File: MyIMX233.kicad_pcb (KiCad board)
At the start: 2 copper layers, 74.1 x 92 mm, 40 parts, among them IC1 iMX233, IC2 DDR_SDRAM_MT46_x16, J1 USB_A, J2 Micro_SD_Card, SW1 SWITCH_PUSHBUTTON, Y1 24Mhz

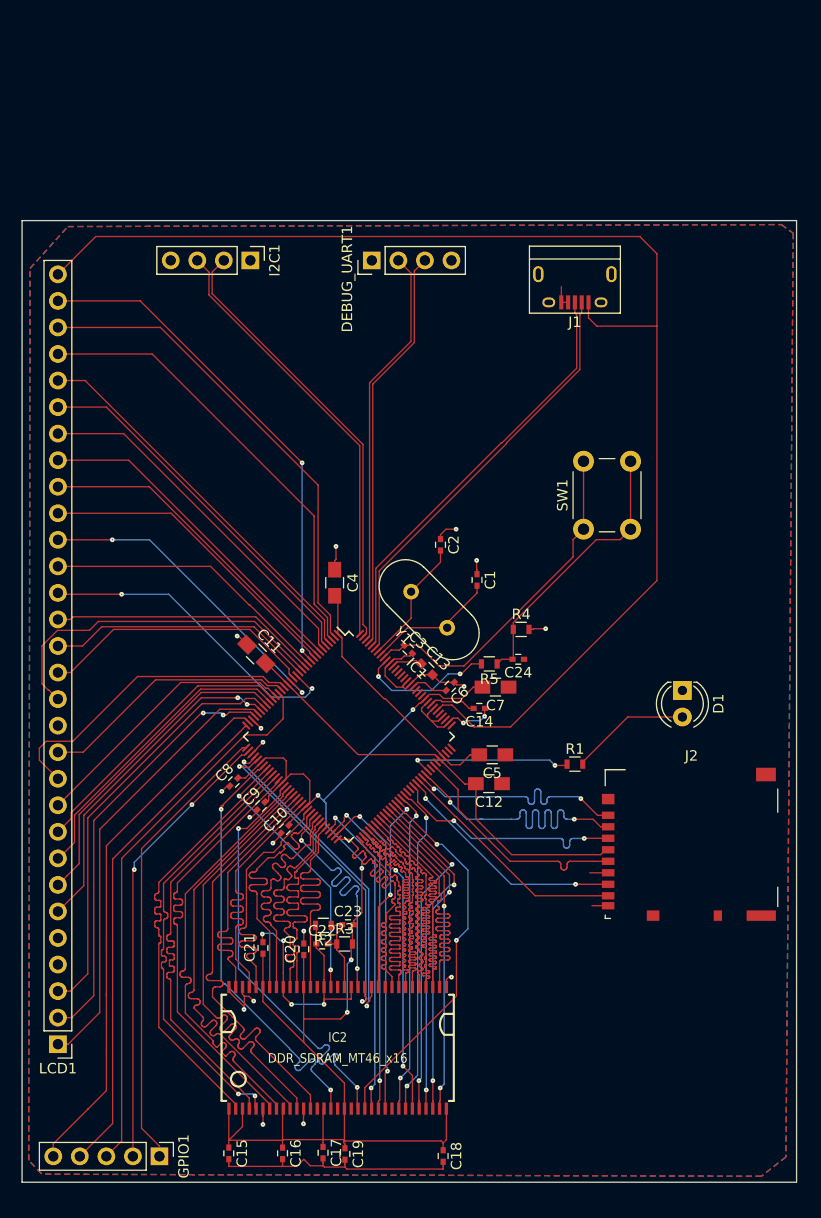
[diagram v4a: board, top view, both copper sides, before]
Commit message: updated with step files new battery and inductor diag
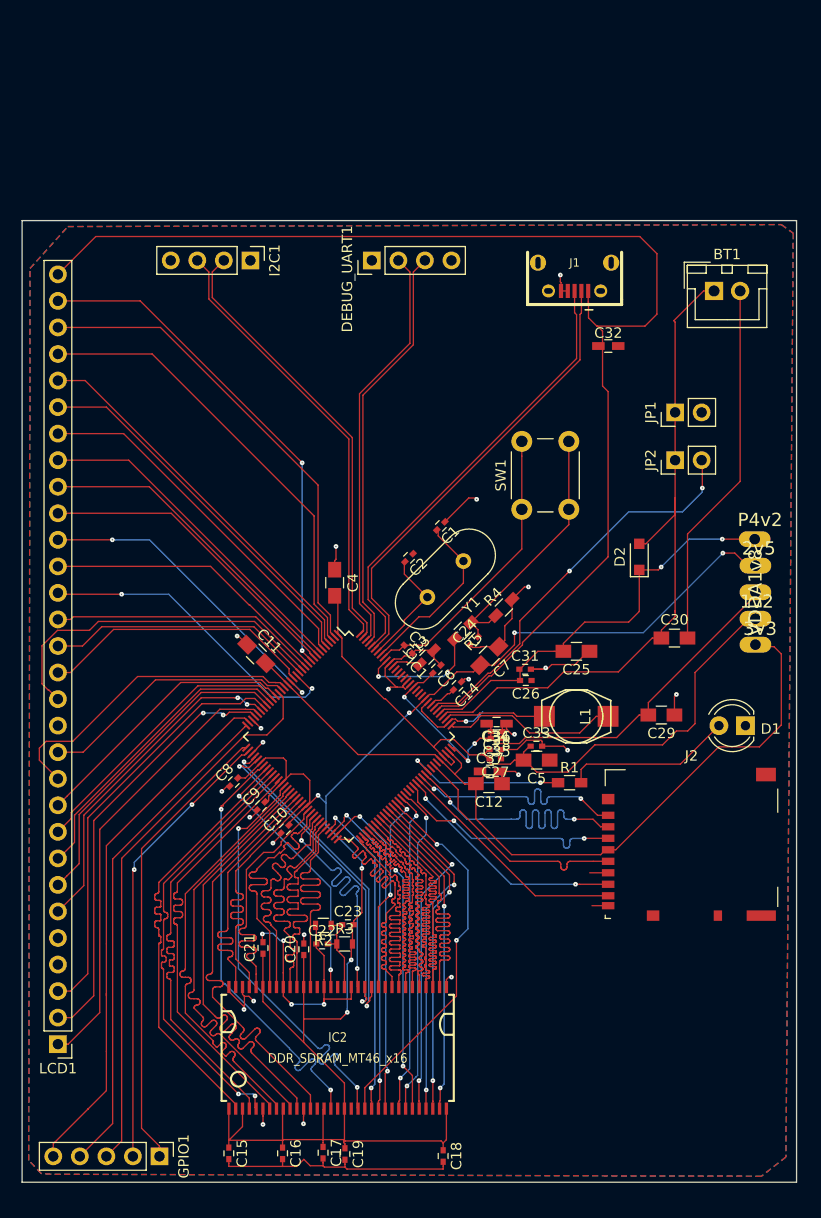
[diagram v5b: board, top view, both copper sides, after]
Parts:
- added BT1: Battery, Connectors_JST:JST_XH_B02B-XH-A_02x2.50mm_Straight, F.Cu at (131.9, 56.3)
- added C25: 22u, Capacitors_SMD:C_0805_HandSoldering, F.Cu at (118.8, 90.7)
- added C26: 1u, Capacitors_SMD:C_0402, F.Cu at (113.9, 93.5)
- added C27: 1u, Capacitors_SMD:C_0402, F.Cu at (111.0, 101.0)
- added C28: 10n, Capacitors_SMD:C_0402, F.Cu at (111.1, 98.4)
- added C29: 47u, Capacitors_SMD:C_0805_HandSoldering, F.Cu at (126.9, 96.8)
- added C30: 47u, Capacitors_SMD:C_0805_HandSoldering, F.Cu at (128.1, 89.5)
- added C31: 100n, Capacitors_SMD:C_0402, F.Cu at (113.9, 92.5)
- added C32: 4.7uf, Capacitors_SMD:C_0603_HandSoldering, F.Cu at (121.8, 61.5)
- added C33: 100n, Capacitors_SMD:C_0402, F.Cu at (114.9, 99.8)
- added C34: 10n, Capacitors_SMD:C_0402, F.Cu at (111.0, 100.1)
- added C35: 100n, Capacitors_SMD:C_0402, F.Cu at (111.1, 99.1)
- added C36: 1u, Capacitors_SMD:C_0603_HandSoldering, F.Cu at (111.1, 97.7)
- added C37: 1u, Capacitors_SMD:C_0603_HandSoldering, F.Cu at (110.5, 102.2)
- added D2: D_Schottky, Diodes_SMD:D_SOD-323_HandSoldering, F.Cu at (124.8, 81.7)
- added JP1: Jumper, Pin_Headers:Pin_Header_Straight_1x02_Pitch2.54mm, F.Cu at (128.2, 67.9)
- added JP2: Jumper, Pin_Headers:Pin_Header_Straight_1x02_Pitch2.54mm, F.Cu at (128.2, 72.5)
- added L1: 22uH, mylib:Bourns22uh6x6mm, F.Cu at (118.7, 97.0)
- added P1: P4v2, iMX233-OLinuXino-NANO_Rev_B:GOGO_TESTPAD40_OBLONG, F.Cu at (135.8, 80.0)
- added P2: 1v2, iMX233-OLinuXino-NANO_Rev_B:GOGO_TESTPAD40_OBLONG, F.Cu at (135.9, 87.6)
- added P3: VDDA1v8, iMX233-OLinuXino-NANO_Rev_B:GOGO_TESTPAD40_OBLONG, F.Cu at (135.9, 85.1)
- added P4: 2v5, iMX233-OLinuXino-NANO_Rev_B:GOGO_TESTPAD40_OBLONG, F.Cu at (135.9, 82.5)
- added P5: 3v3, iMX233-OLinuXino-NANO_Rev_B:GOGO_TESTPAD40_OBLONG, F.Cu at (135.9, 90.1)
- C12: value 22u -> 100n
- C13: footprint Capacitors_SMD:C_0603 -> Capacitors_SMD:C_0603_HandSoldering
- IC2: footprint opendous:TSOP66_JEDEC_DDR_SDRAM -> mylib:TSOP66_JEDEC_DDR_SDRAM
- J1: footprint mylib:USB_Micro-B_MOLEX_105017-0001 -> conn-fci:CONN-10118194-0001LF-FCI
- R1, R4, R5: footprint Resistors_SMD:R_0603 -> Resistors_SMD:R_0603_HandSoldering
- moved D1 6.91 mm to (134.9, 97.9), turned to 180 degrees
- moved Y1 6.57 mm to (108.0, 82.1), turned to 225 degrees
- moved C1 6.23 mm to (105.8, 78.7), turned to 225 degrees
- moved SW1 6.21 mm to (113.5, 77.2)
- moved C24 4.60 mm to (109.0, 89.7), turned to 45 degrees
- moved C5 4.27 mm to (115.0, 101.2)
- moved R5 4.07 mm to (107.9, 88.8), turned to 225 degrees
- moved C2 3.26 mm to (102.7, 81.8), turned to 225 degrees
- moved C7 3.04 mm to (110.4, 91.2), turned to 225 degrees
- moved C14 3.01 mm to (107.4, 94.0), turned to 225 degrees
- moved R4 2.67 mm to (111.8, 86.6), turned to 45 degrees
- moved J1 2.45 mm to (118.6, 53.6)
- moved C6 2.08 mm to (105.4, 92.5)
- moved R1 1.85 mm to (118.1, 103.3)
- moved C13 1.14 mm to (104.5, 91.3), turned to 45 degrees
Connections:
- IC1 pad 100: GND -> /+VE
- IC1 pad 103: GND -> Net-(IC1-Pad103)
- IC1 pad 94: Net-(IC1-Pad94) -> 1V2_SYS
- IC1 pad 95: Net-(IC1-Pad95) -> 3v3_SYS
- IC1 pad 96: Net-(IC1-Pad96) -> VDDA_SYS
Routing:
- net /+VE: track 0.00 -> 66.3 mm
- net VDDA_SYS: track 3.64 -> 52.4 mm, vias 0 -> 3
- net 1V2_SYS: track 23.9 -> 66.6 mm
- net Net-(C25-Pad2): track 0.00 -> 40.5 mm, vias 0 -> 2
- net Net-(IC1-Pad103): track 0.00 -> 38.6 mm, vias 0 -> 2
- net 3v3_SYS: track 42.6 -> 78.1 mm
- net Net-(BT1-Pad2): track 0.00 -> 35.3 mm
- net 2V5_SYS: track 138.1 -> 170.3 mm, vias 5 -> 7
- net GND: track 107.1 -> 136.4 mm, vias 23 -> 28
- net Net-(IC1-Pad97): track 0.00 -> 16.9 mm
- net Net-(IC1-Pad99): track 0.60 -> 9.83 mm
- net +5V: track 127.1 -> 120.3 mm
- net VDDXTAL_SYS: track 33.3 -> 27.8 mm
- net Net-(D1-Pad2): track 11.5 -> 16.2 mm
- net Net-(C1-Pad2): track 12.6 -> 16.7 mm
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
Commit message: pcb-1.0
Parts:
- added C39: 100n, Capacitors_SMD:C_0402, F.Cu at (111.1, 104.7)
- added C40: 10n, Capacitors_SMD:C_0402, F.Cu at (111.1, 103.6)
- added D3: LED, LEDs:LED_0603, F.Cu at (106.8, 60.9)
- added R6: 10k, Resistors_SMD:R_0603_HandSoldering, F.Cu at (114.9, 60.8)
- added R7: 1k, Resistors_SMD:R_0603_HandSoldering, F.Cu at (106.9, 65.8)
- added REF**: 1pin, Connectors:1pin, F.Cu at (130.1, 133.1)
- C12: footprint Capacitors_SMD:C_0805_HandSoldering -> Capacitors_SMD:C_0402
- P1, P2, P3, P4, P5: footprint iMX233-OLinuXino-NANO_Rev_B:GOGO_TESTPAD40_OBLONG -> iMX233-OLinuXino-NANO_Rev_BEagle:GOGO_TESTPAD2
- R1: value R -> 1k
- moved C11 28.0 mm to (111.7, 106.1), turned to 180 degrees
- moved C12 25.2 mm to (88.2, 91.4), turned to 315 degrees
- moved R1 8.84 mm to (126.6, 100.7)
- moved C33 2.54 mm to (114.9, 102.4)
- moved C5 0.34 mm to (115.1, 100.8)
- moved P1 0.06 mm to (135.9, 80.0)
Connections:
- BT1 pad 2: Net-(BT1-Pad2) -> GND
- C30 pad 2: Net-(BT1-Pad2) -> GND
- I2C1 pad 1: Net-(I2C1-Pad1) -> +5V
- IC1 pad 89: Net-(IC1-Pad89) -> Net-(DEBUG_UART1-Pad1)
- J1 pad 4: GND -> Net-(J1-Pad4)
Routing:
- net Net-(DEBUG_UART1-Pad1): track 0.00 -> 55.0 mm, vias 0 -> 2
- net Net-(IC1-Pad91): track 0.00 -> 50.6 mm, vias 0 -> 2
- net GND: track 136.4 -> 177.3 mm
- net Net-(BT1-Pad2): track 35.3 -> 0.00 mm
- net Net-(D1-Pad2): track 16.2 -> 6.34 mm
- net Net-(IC1-Pad88): track 15.8 -> 25.4 mm
- net Net-(J1-Pad4): track 0.00 -> 5.38 mm
- net Net-(IC1-Pad3): track 43.5 -> 38.5 mm
- net 3v3_SYS: track 78.1 -> 82.9 mm
- net 1V2_SYS: track 66.6 -> 70.0 mm
- net Net-(D3-Pad2): track 0.00 -> 3.10 mm
- net +5V: track 120.3 -> 122.6 mm
- net VDDA_SYS: track 52.4 -> 54.0 mm
- net 2V5_SYS: track 170.3 -> 171.3 mm
